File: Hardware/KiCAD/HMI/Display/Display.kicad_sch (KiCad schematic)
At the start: 21 parts, among them IC2 AP2112, IC4 APX803-SAG, Q2 MICROSD, Q3 BSS138, U1 74HC4050PWR, X1 EYE_SPI_DISPLAY_FLIP

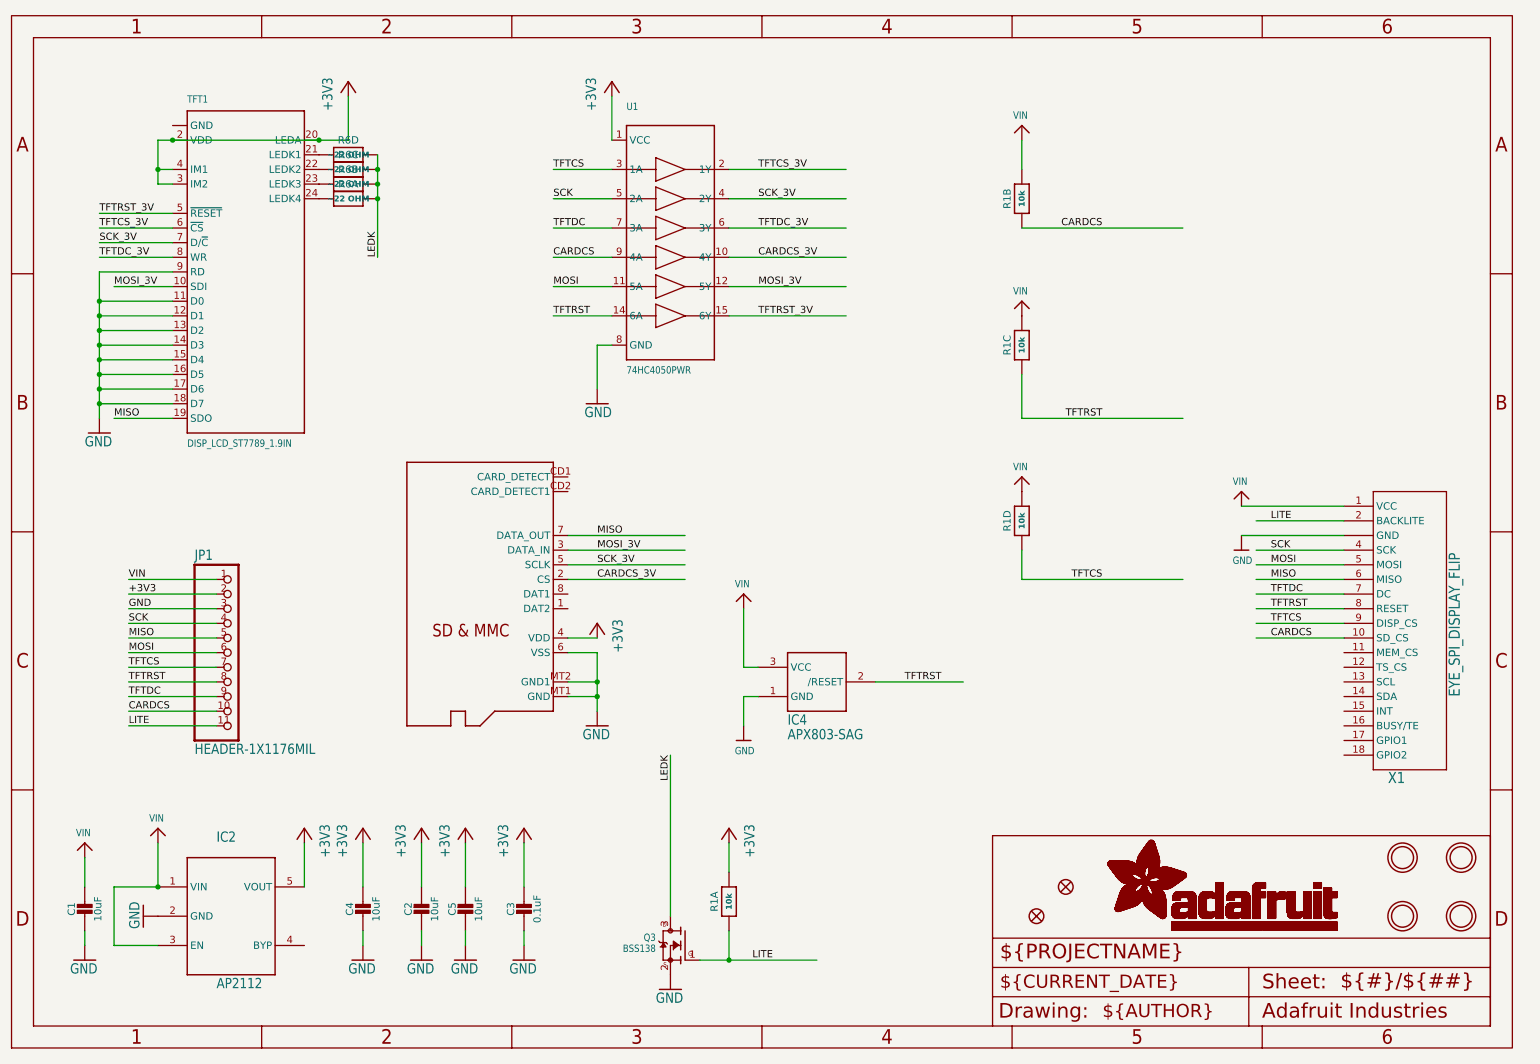
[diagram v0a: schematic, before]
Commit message: feat: capture EYESPI display connectors #15
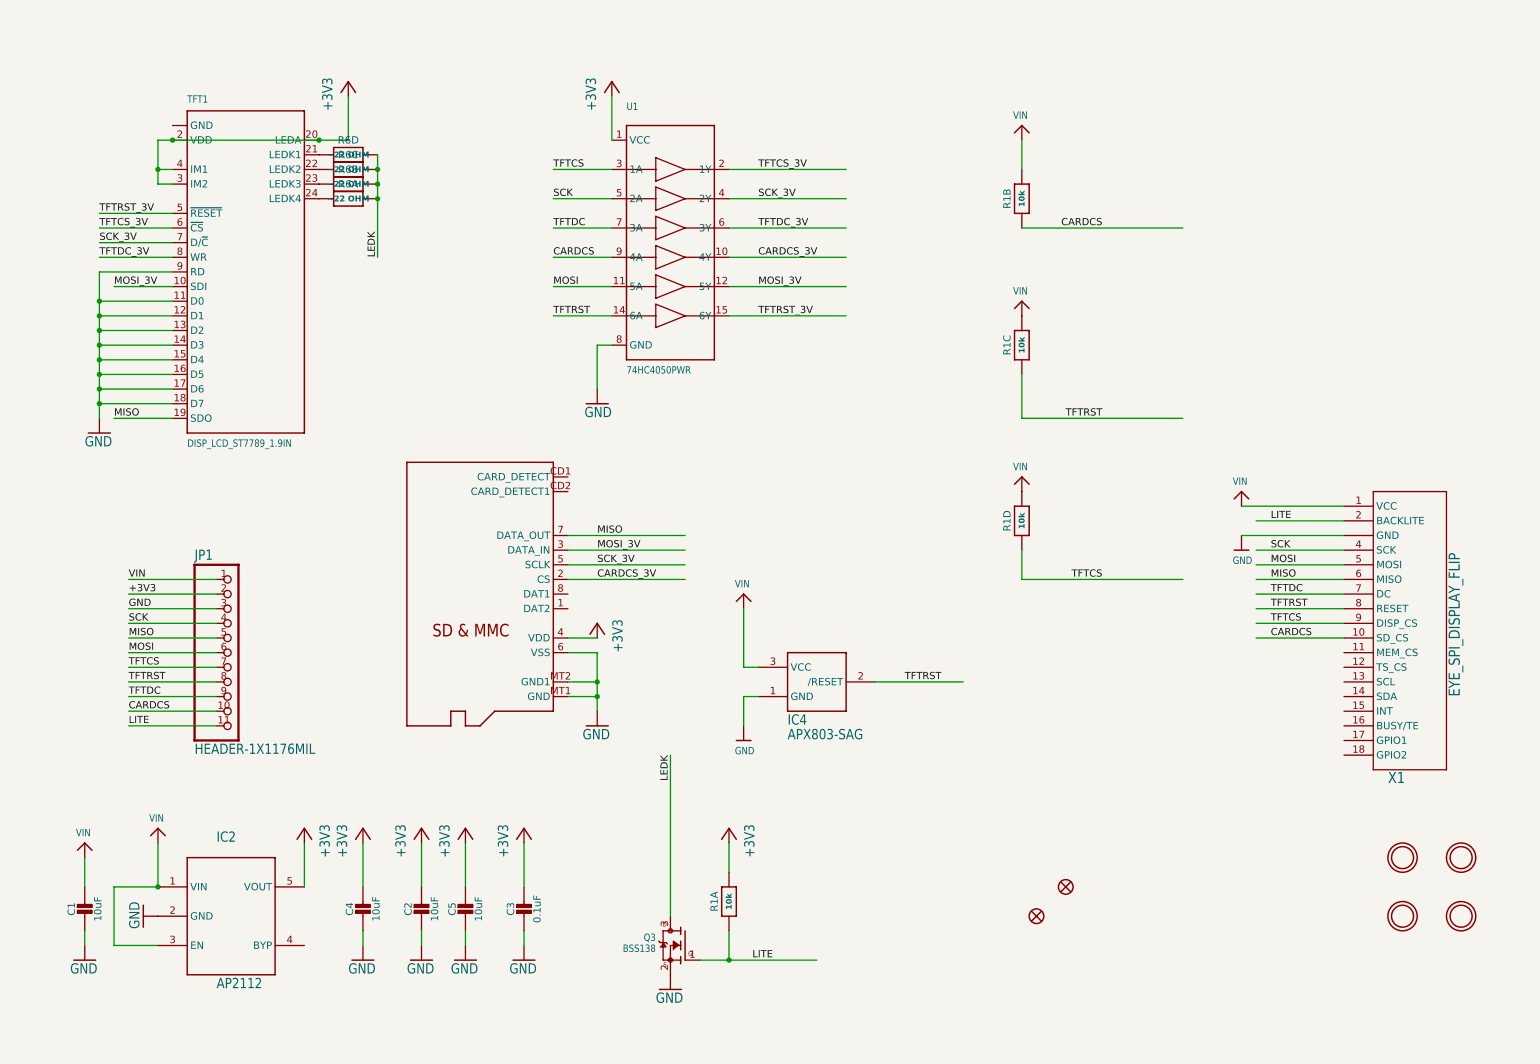
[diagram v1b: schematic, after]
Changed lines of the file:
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@@
 (kicad_sch
-	(version 20231120)
+	(version 20250114)
 	(generator "eeschema")
-	(generator_version "8.0")
+	(generator_version "9.0")
 	(paper "User" 298.45 217.322)
 	(junction
@@
 	(label "MOSI"
 		(at 40.64 129.54 0)
-		(fields_autoplaced yes)
 		(effects
 			(font
@@
 	(label "CARDCS"
 		(at 209.55 55.88 180)
-		(fields_autoplaced yes)
 		(effects
 			(font
@@
 	(label "TFTDC_3V"
 		(at 149.86 55.88 0)
-		(fields_autoplaced yes)
 		(effects
 			(font
@@
 	(label "SCK_3V"
 		(at 35.56 58.42 0)
-		(fields_autoplaced yes)
 		(effects
 			(font
@@
 	(label "TFTDC"
 		(at 238.76 119.38 0)
-		(fields_autoplaced yes)
 		(effects
 			(font
@@
 	(label "TFTDC"
 		(at 40.64 137.16 0)
-		(fields_autoplaced yes)
 		(effects
 			(font
@@
 	(label "SCK"
 		(at 40.64 124.46 0)
-		(fields_autoplaced yes)
 		(effects
 			(font
@@
 	(label "CARDCS"
 		(at 40.64 139.7 0)
-		(fields_autoplaced yes)
 		(effects
 			(font
@@
 	(label "TFTCS_3V"
 		(at 35.56 55.88 0)
-		(fields_autoplaced yes)
 		(effects
 			(font
@@
 	(label "SCK"
 		(at 114.3 50.8 0)
-		(fields_autoplaced yes)
 		(effects
 			(font
@@
 	(label "SCK"
 		(at 238.76 111.76 0)
-		(fields_autoplaced yes)
 		(effects
 			(font
@@
 	(label "CARDCS"
 		(at 114.3 60.96 0)
-		(fields_autoplaced yes)
 		(effects
 			(font
@@
 	(label "TFTCS_3V"
 		(at 149.86 45.72 0)
-		(fields_autoplaced yes)
 		(effects
 			(font
@@
 	(label "VIN"
 		(at 40.64 116.84 0)
-		(fields_autoplaced yes)
 		(effects
 			(font
@@
 	(label "LEDK"
 		(at 134.62 147.32 270)
-		(fields_autoplaced yes)
 		(effects
 			(font
@@
 	(label "MOSI_3V"
 		(at 121.92 111.76 0)
-		(fields_autoplaced yes)
 		(effects
 			(font
@@
 	(label "MISO"
 		(at 40.64 127 0)
-		(fields_autoplaced yes)
 		(effects
 			(font
@@
 	(label "MOSI"
 		(at 238.76 114.3 0)
-		(fields_autoplaced yes)
 		(effects
 			(font
@@
 	(label "CARDCS_3V"
 		(at 149.86 60.96 0)
-		(fields_autoplaced yes)
 		(effects
 			(font
@@
 	(label "SCK_3V"
 		(at 149.86 50.8 0)
-		(fields_autoplaced yes)
 		(effects
 			(font
@@
 	(label "LITE"
 		(at 238.76 106.68 0)
-		(fields_autoplaced yes)
 		(effects
 			(font
@@
 	(label "MOSI_3V"
 		(at 38.1 66.04 0)
-		(fields_autoplaced yes)
 		(effects
 			(font
@@
 	(label "TFTDC"
 		(at 114.3 55.88 0)
-		(fields_autoplaced yes)
 		(effects
 			(font
@@
 	(label "TFTRST_3V"
 		(at 35.56 53.34 0)
-		(fields_autoplaced yes)
 		(effects
 			(font
@@
 	(label "TFTRST"
 		(at 209.55 88.9 180)
-		(fields_autoplaced yes)
 		(effects
 			(font
@@
 	(label "TFTRST"
 		(at 175.26 134.62 0)
-		(fields_autoplaced yes)
 		(effects
 			(font
@@
 	(label "TFTRST"
 		(at 238.76 121.92 0)
-		(fields_autoplaced yes)
 		(effects
 			(font
@@
 	(label "TFTCS"
 		(at 209.55 116.84 180)
-		(fields_autoplaced yes)
 		(effects
 			(font
@@
 	(label "MISO"
 		(at 121.92 109.22 0)
-		(fields_autoplaced yes)
 		(effects
 			(font
@@
 	(label "+3V3"
 		(at 40.64 119.38 0)
-		(fields_autoplaced yes)
 		(effects
 			(font
@@
 	(label "SCK_3V"
 		(at 121.92 114.3 0)
-		(fields_autoplaced yes)
 		(effects
 			(font
@@
 	(label "GND"
 		(at 40.64 121.92 0)
-		(fields_autoplaced yes)
 		(effects
 			(font
@@
 	(label "TFTCS"
 		(at 114.3 45.72 0)
-		(fields_autoplaced yes)
 		(effects
 			(font
@@
 	(label "MISO"
 		(at 38.1 88.9 0)
-		(fields_autoplaced yes)
 		(effects
 			(font
@@
 	(label "TFTCS"
 		(at 40.64 132.08 0)
-		(fields_autoplaced yes)
 		(effects
 			(font
@@
 	(label "TFTDC_3V"
 		(at 35.56 60.96 0)
-		(fields_autoplaced yes)
 		(effects
 			(font
@@
 	(label "MISO"
 		(at 238.76 116.84 0)
-		(fields_autoplaced yes)
 		(effects
 			(font
@@
 	(label "TFTRST_3V"
 		(at 149.86 71.12 0)
-		(fields_autoplaced yes)
 		(effects
 			(font
@@
 	(label "LITE"
 		(at 40.64 142.24 0)
-		(fields_autoplaced yes)
 		(effects
 			(font
@@
 	(label "MOSI_3V"
 		(at 149.86 66.04 0)
-		(fields_autoplaced yes)
 		(effects
 			(font
@@
 	(label "CARDCS_3V"
 		(at 121.92 116.84 0)
-		(fields_autoplaced yes)
 		(effects
 			(font
@@
 	(label "LEDK"
 		(at 83.82 60.96 90)
-		(fields_autoplaced yes)
 		(effects
 			(font
@@
 	(label "MOSI"
 		(at 114.3 66.04 0)
-		(fields_autoplaced yes)
 		(effects
 			(font
@@
 	(label "TFTRST"
 		(at 114.3 71.12 0)
-		(fields_autoplaced yes)
 		(effects
 			(font
@@
 	(label "LITE"
 		(at 152.4 182.88 180)
-		(fields_autoplaced yes)
 		(effects
 			(font
@@
 	(label "TFTCS"
 		(at 238.76 124.46 0)
-		(fields_autoplaced yes)
 		(effects
 			(font
@@
 	(label "CARDCS"
 		(at 238.76 127 0)
-		(fields_autoplaced yes)
 		(effects
 			(font
@@
 	(label "TFTRST"
 		(at 40.64 134.62 0)
-		(fields_autoplaced yes)
 		(effects
 			(font
@@
 	)
 	(symbol
-		(lib_id "Display-eagle-import:FRAME_A4_ADAFRUIT")
-		(at 20.32 198.12 0)
-		(unit 1)
-		(exclude_from_sim no)
-		(in_bom yes)
-		(on_board yes)
-		(dnp no)
-		(property "Reference" "#U$6"
-			(at 20.32 198.12 0)
-			(effects
-				(font
-					(size 1.27 1.27)
-				)
-				(hide yes)
-			)
-		)
-		(property "Value" "FRAME_A4_ADAFRUIT"
-			(at 20.32 198.12 0)
-			(effects
-				(font
-					(size 1.27 1.27)
-				)
-				(hide yes)
-			)
-		)
-		(property "Footprint" ""
-			(at 20.32 198.12 0)
-			(effects
-				(font
-					(size 1.27 1.27)
-				)
-				(hide yes)
-			)
-		)
-		(property "Datasheet" ""
-			(at 20.32 198.12 0)
-			(effects
-				(font
-					(size 1.27 1.27)
-				)
-				(hide yes)
-			)
-		)
-		(property "Description" ""
-			(at 20.32 198.12 0)
-			(effects
-				(font
-					(size 1.27 1.27)
-				)
-				(hide yes)
-			)
-		)
-		(instances
-			(project ""
-				(path "/af66a13c-ed98-483d-86d1-8d6f28143c3a"
-					(reference "#U$6")
-					(unit 1)
-				)
-			)
-		)
-	)
-	(symbol
 		(lib_id "Display-eagle-import:GND")
 		(at 121.92 86.36 0)
@@
 		)
 	)
+	(embedded_fonts no)
 )
